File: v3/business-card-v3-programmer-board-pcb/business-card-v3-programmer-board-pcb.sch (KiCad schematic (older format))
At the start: 17 parts, among them J1 Pogo_Pin_Conn, J2 Power_TP, J3 Programmer_Conn, J4 Jack-DC, SW1 RST, U1 LM2904, U2 L7805CV

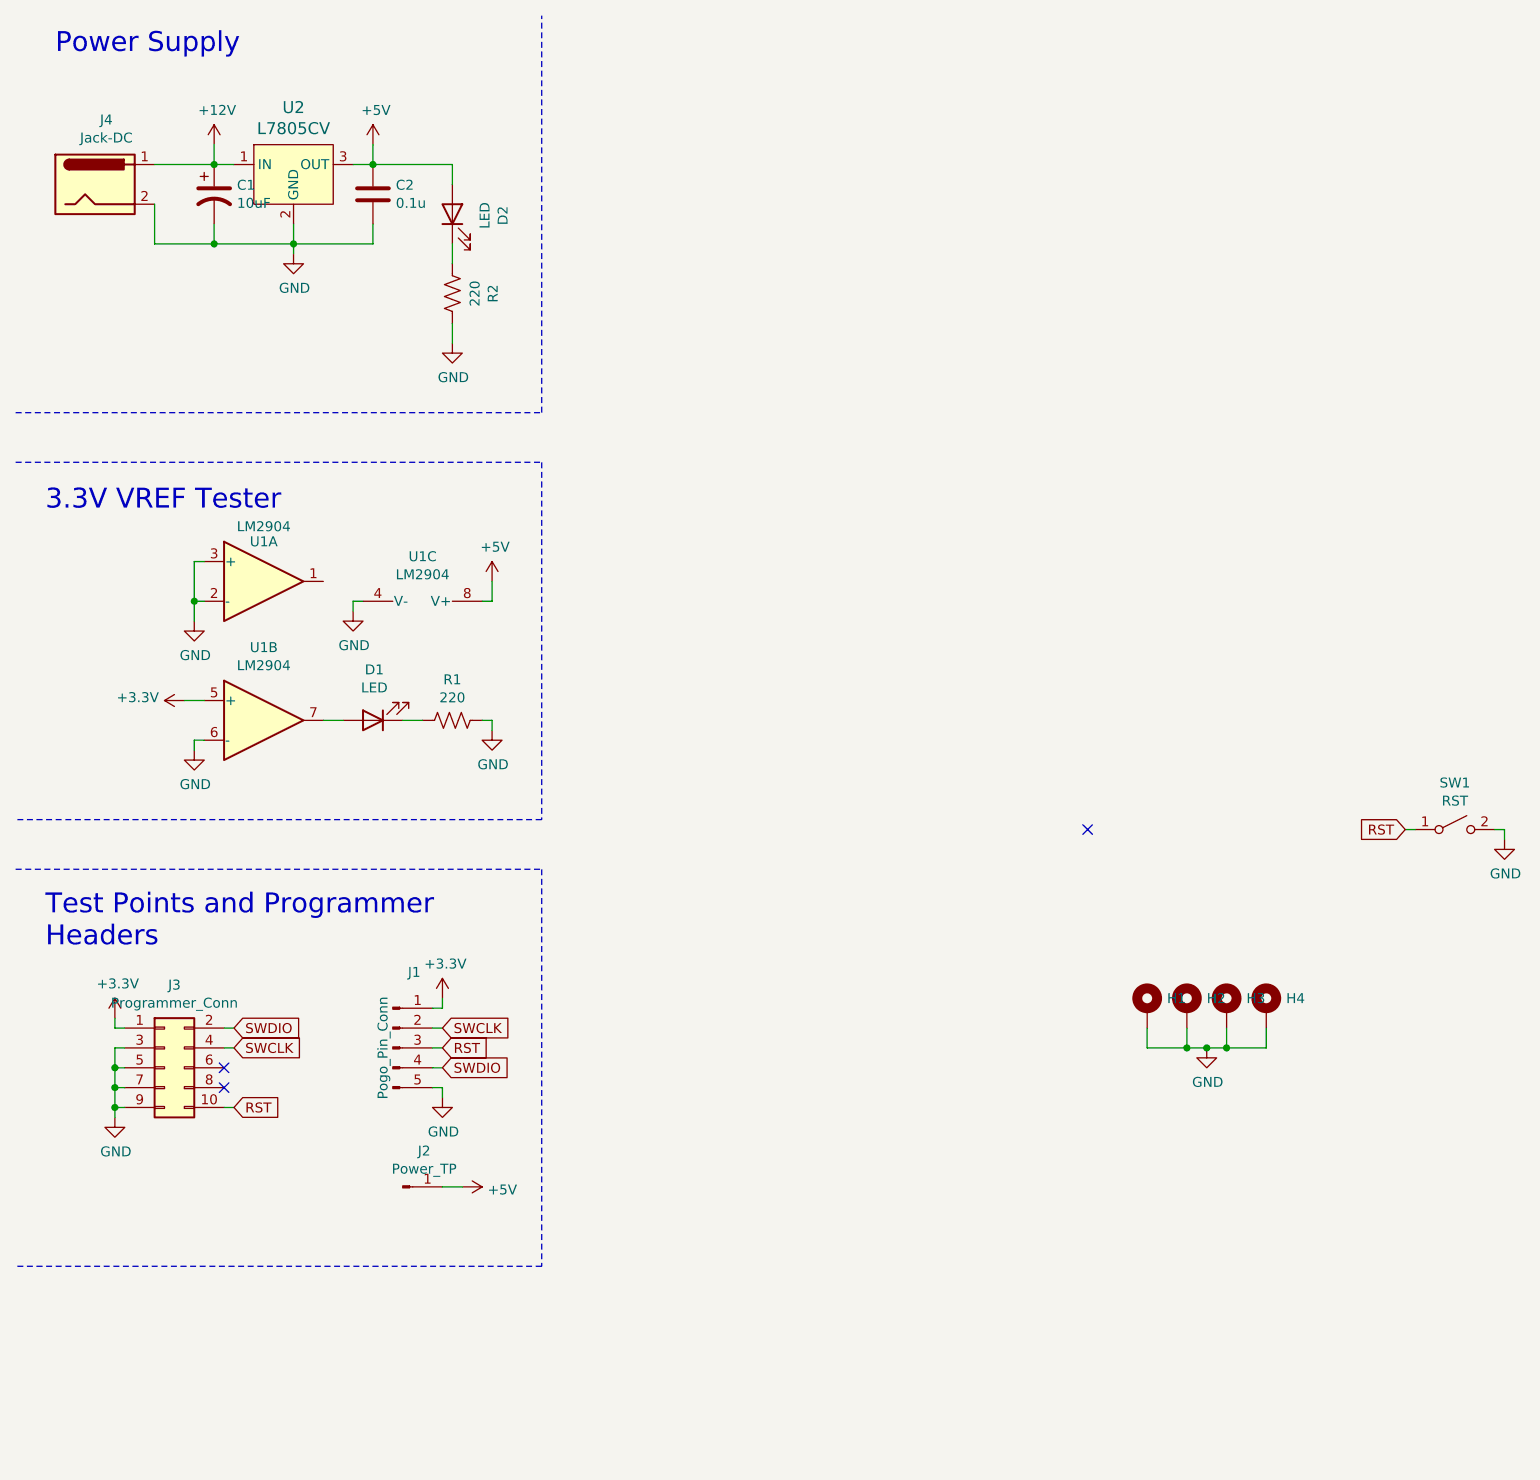
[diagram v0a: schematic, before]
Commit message: move the programmer board files up a level
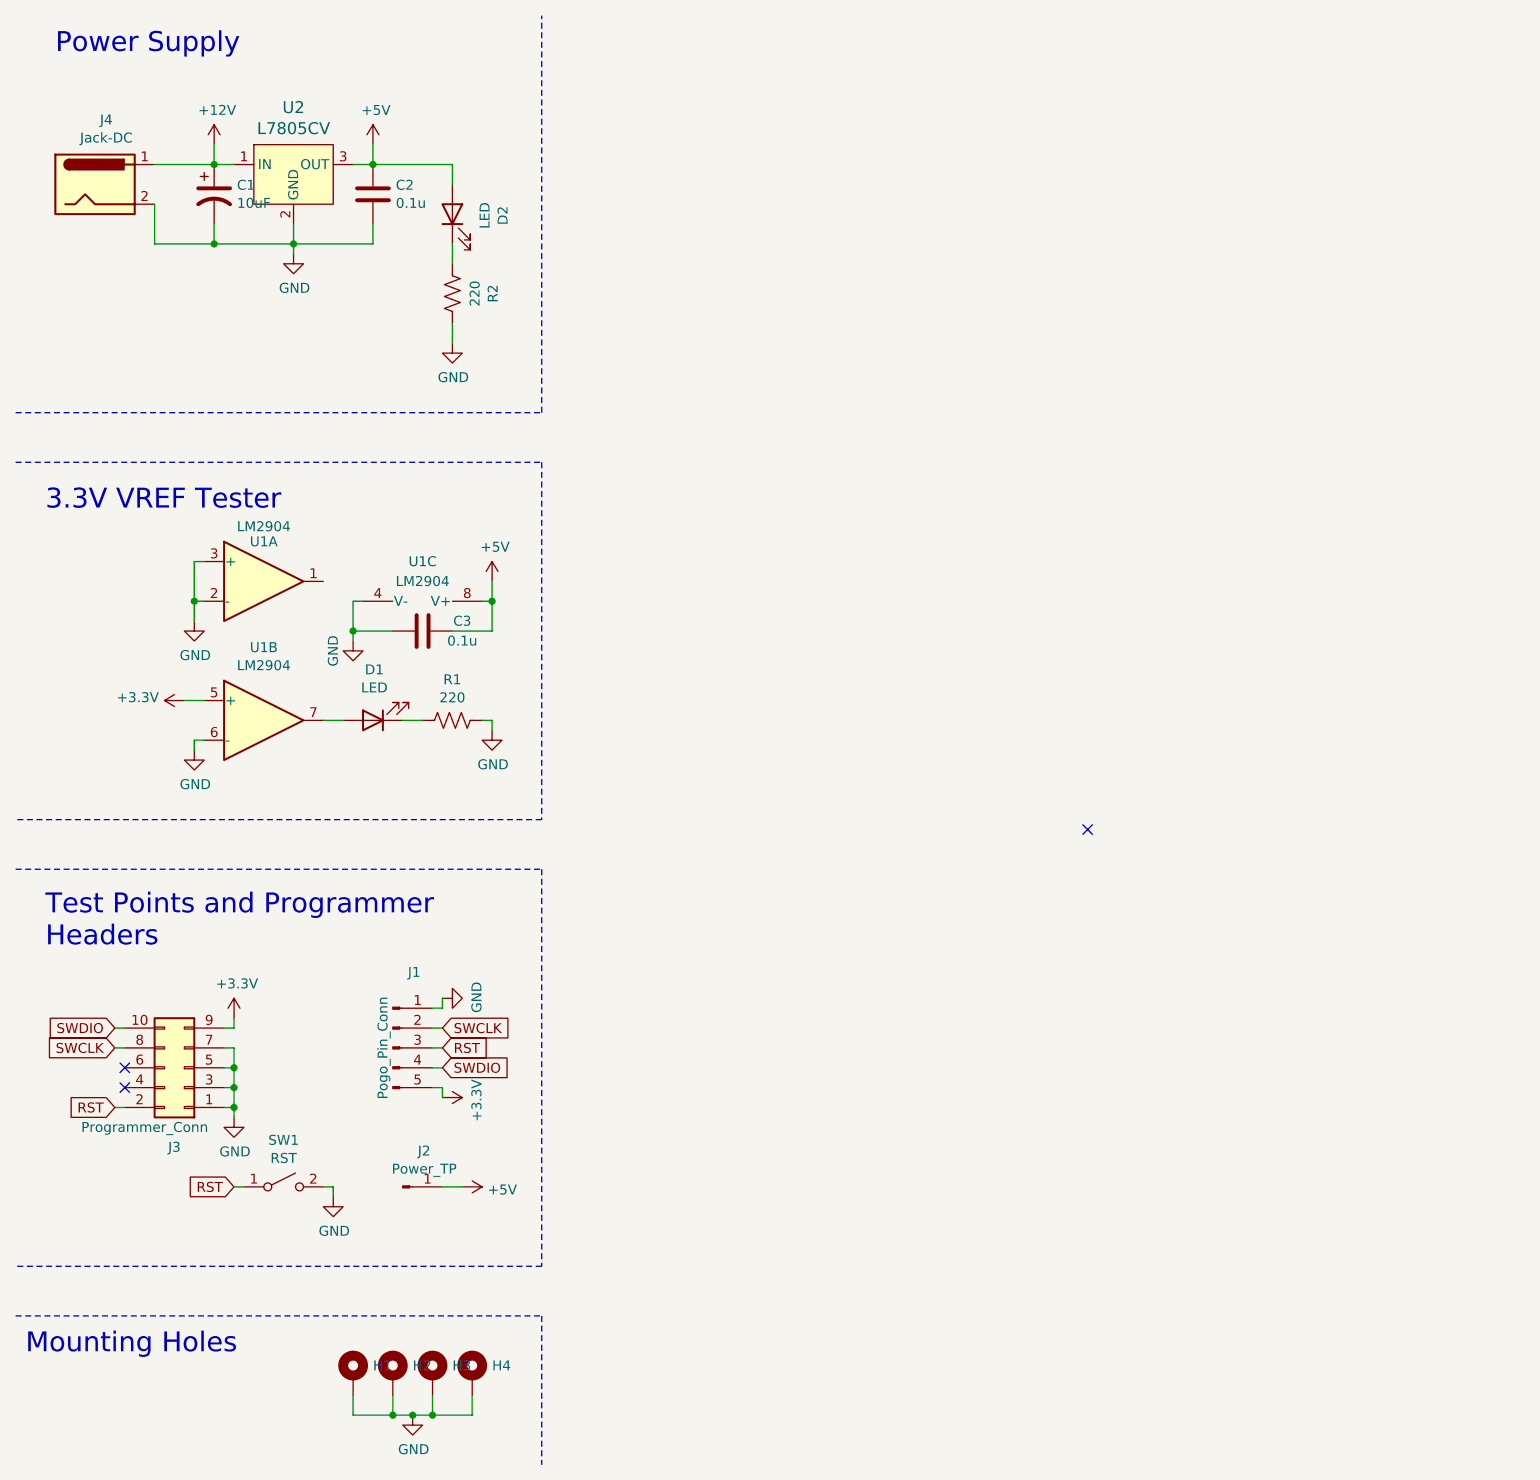
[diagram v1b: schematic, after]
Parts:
- added C3: 0.1u, Capacitor_SMD:C_0603_1608Metric, symbol Device:C
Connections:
- net +3V3: now also J1.5 (Pin_5), J3.9 (Pin_9); no longer J1.1 (Pin_1), J3.1 (Pin_1)
- net +5V: now also C3.1
- net GND: now also J1.1 (Pin_1), J3.1 (Pin_1), C3.2; no longer J1.5 (Pin_5), J3.9 (Pin_9)
- net RST: now also J3.2 (Pin_2); no longer J3.10 (Pin_10)
- net SWCLK: now also J3.8 (Pin_8); no longer J3.4 (Pin_4)
- net SWDIO: now also J3.10 (Pin_10); no longer J3.2 (Pin_2)
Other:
- note added: "Mounting Holes"
- moved on the sheet: H1, H2, H3, H4, SW1
